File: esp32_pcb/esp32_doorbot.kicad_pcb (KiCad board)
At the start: 2 copper layers, 29.2 x 51.8 mm, 18 parts, among them J1 Conn_01x07_Male, J2 Conn_01x02_Female, J3 Barrel_Jack, J4 WROOM32_1, J5 WROOM32_2, Q1 2N7002E, U1 L7805, U2 74LVC2T45DC

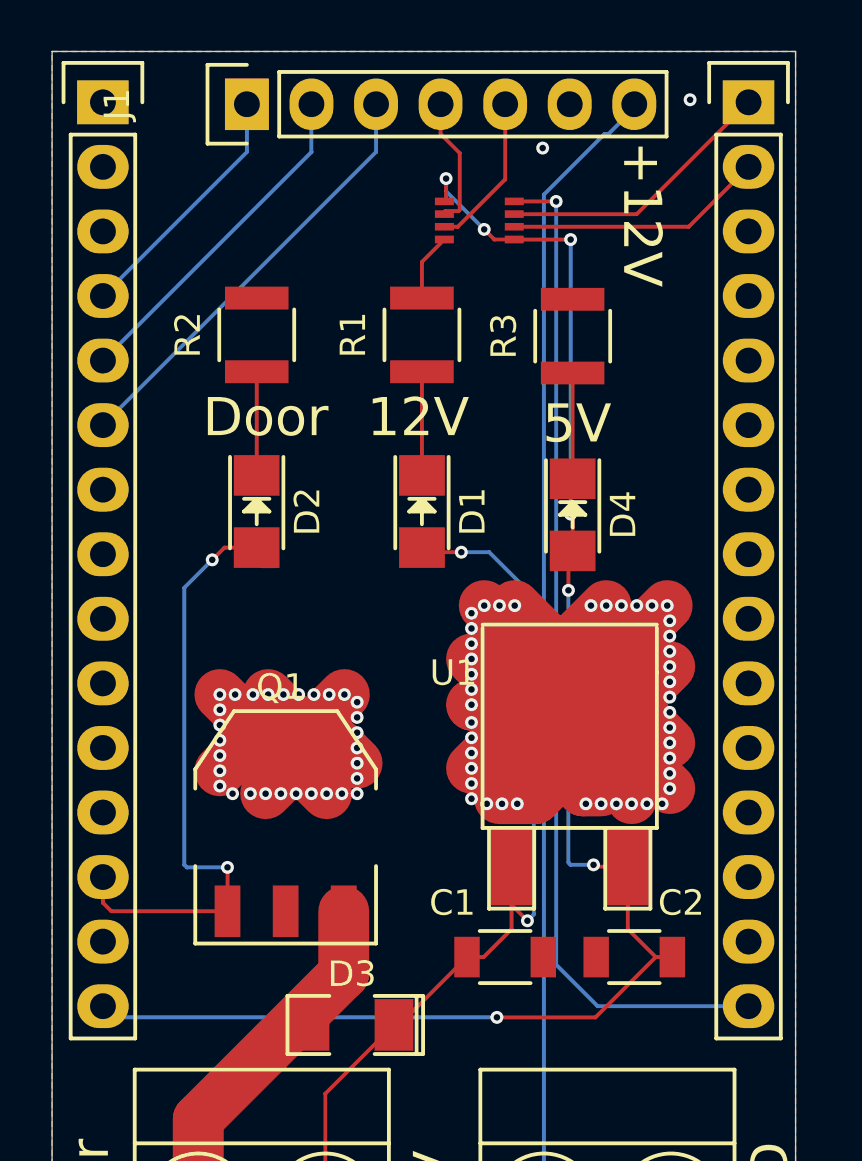
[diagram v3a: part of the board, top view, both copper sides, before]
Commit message: Switch to voltage divider instead of logic level converter
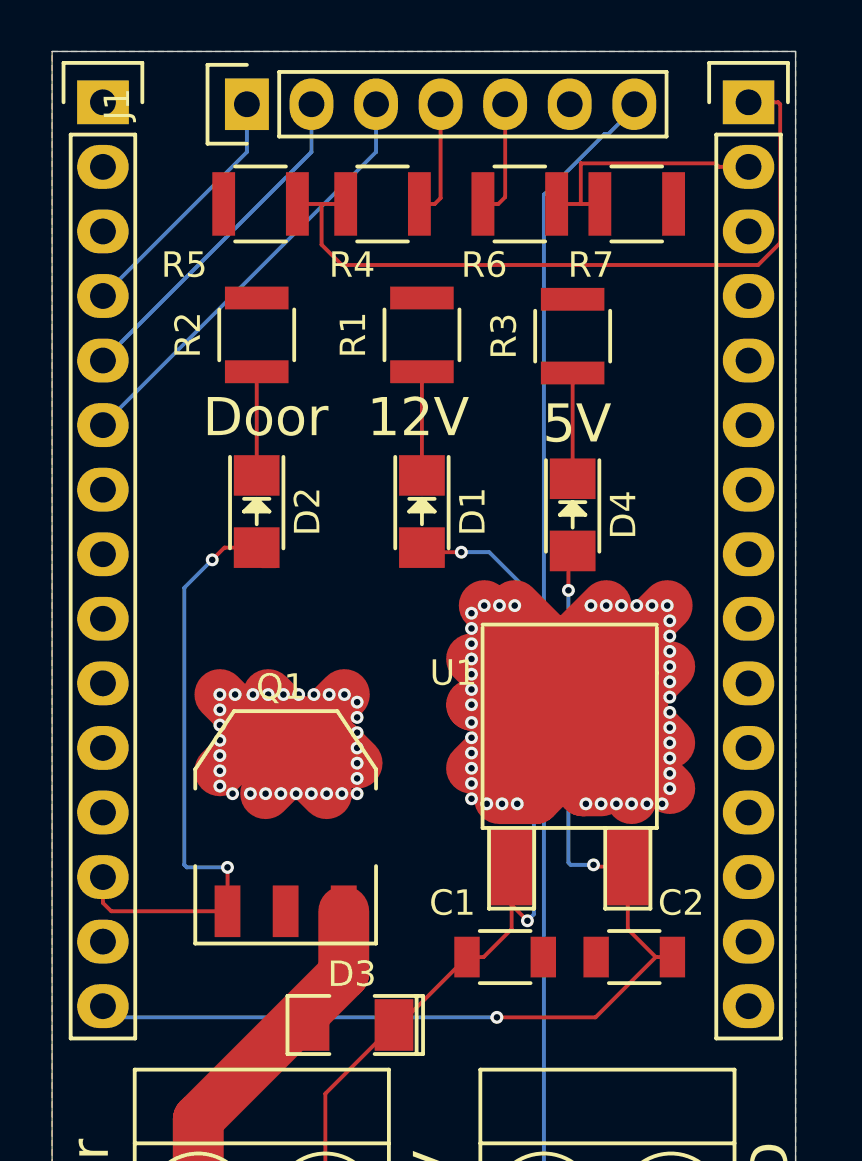
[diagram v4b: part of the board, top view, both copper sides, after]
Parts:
- removed REF**: Bodgery, custom:Bodgery
- removed U2: 74LVC2T45DC, tinkerforge-kicad:VSSOP8
- added R4: 1k, Resistors_SMD:R_1210, F.Cu at (111.0, 104.0)
- added R5: 2k, Resistors_SMD:R_1210, F.Cu at (106.2, 104.0)
- added R6: 1k, Resistors_SMD:R_1210, F.Cu at (116.4, 104.0)
- added R7: 2k, Resistors_SMD:R_1210, F.Cu at (121.0, 104.0)
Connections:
- J4 pad 1: Net-(J4-Pad1) -> (no net)
- J4 pad 10: Net-(J4-Pad10) -> (no net)
- J4 pad 11: Net-(J4-Pad11) -> (no net)
- J4 pad 12: Net-(J4-Pad12) -> (no net)
- J4 pad 2: Net-(J4-Pad2) -> (no net)
- J4 pad 3: Net-(J4-Pad3) -> (no net)
- J4 pad 7: Net-(J4-Pad7) -> (no net)
- J4 pad 8: Net-(J4-Pad8) -> (no net)
- J4 pad 9: Net-(J4-Pad9) -> (no net)
- J5 pad 10: Net-(J5-Pad10) -> (no net)
- J5 pad 11: Net-(J5-Pad11) -> (no net)
- J5 pad 12: Net-(J5-Pad12) -> (no net)
- J5 pad 13: Net-(J5-Pad13) -> (no net)
- J5 pad 15: 3.3V -> (no net)
- J5 pad 3: Net-(J5-Pad3) -> (no net)
- J5 pad 4: Net-(J5-Pad4) -> (no net)
- J5 pad 5: Net-(J5-Pad5) -> (no net)
- J5 pad 6: Net-(J5-Pad6) -> (no net)
- J5 pad 7: Net-(J5-Pad7) -> (no net)
- J5 pad 8: Net-(J5-Pad8) -> (no net)
- J5 pad 9: Net-(J5-Pad9) -> (no net)
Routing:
- net 3.3V: track 39.9 -> 0.00 mm, vias 1 -> 0
- net 5V: track 61.7 -> 42.3 mm, vias 7 -> 3
- net WIEGAND_OUT2: track 11.0 -> 29.0 mm
- net GND: track 85.1 -> 82.4 mm, vias 75 -> 73
- net WIEGAND_IN1: track 6.12 -> 4.64 mm
- net WIEGAND_IN2: track 5.19 -> 4.62 mm
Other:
- board text added: "ESP32 Doorbot v4 By Timm Murray Copyright © 2021 BY-CC"
- board text removed: "ESP32 Doorbot v3 By Timm Murray Copyright © 2021 BY-CC"

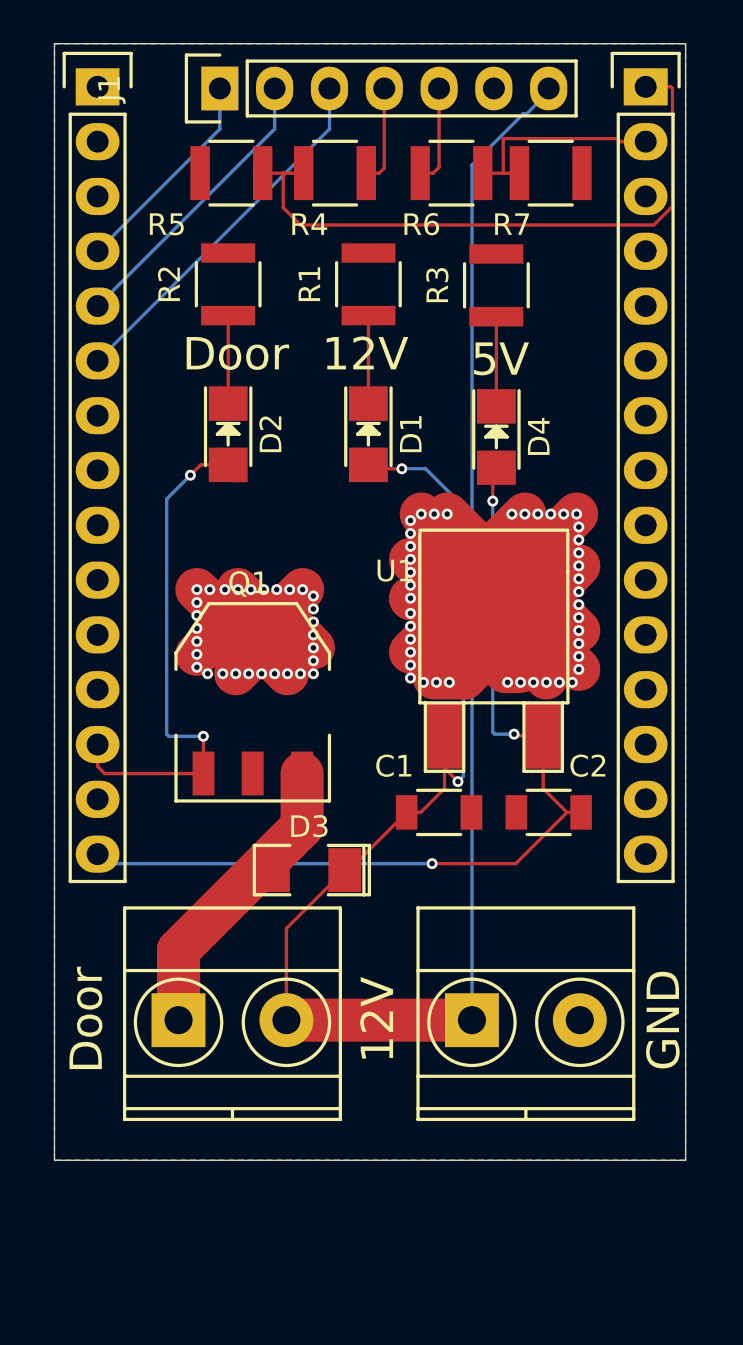
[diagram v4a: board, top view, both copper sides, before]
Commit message: Correct mosfet pinout (for real this time)
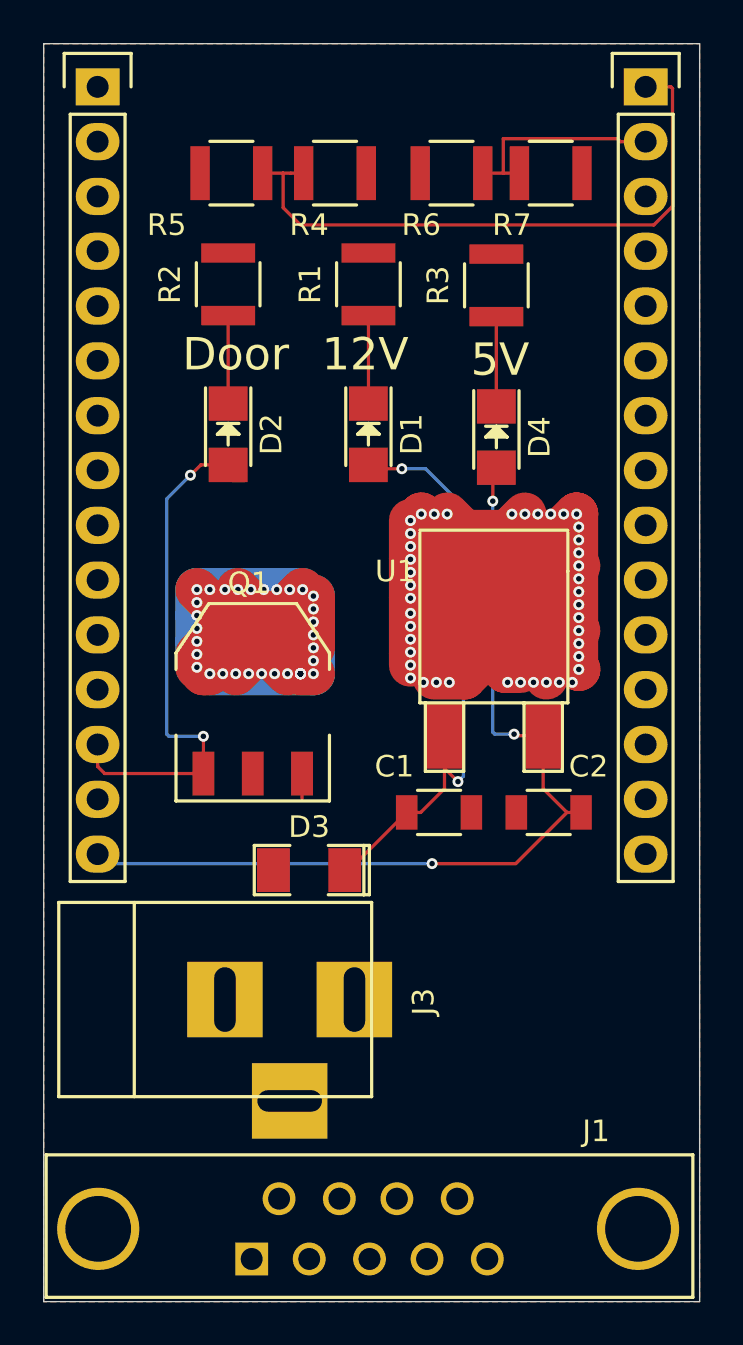
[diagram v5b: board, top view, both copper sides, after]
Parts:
- removed J2: Conn_01x02_Female, Terminal_Blocks:TerminalBlock_Pheonix_MKDS1.5-2pol
- J1: value Conn_01x07_Male -> DB9_Male; footprint Pin_Headers:Pin_Header_Straight_1x07 -> Connect:DB9FD
- J3: footprint Terminal_Blocks:TerminalBlock_Pheonix_MKDS1.5-2pol -> Connect:BARREL_JACK
- Q1: value 2N7002E -> ZVN4206GVTA
- moved J1 53.2 mm to (112.6, 152.8), turned to 180 degrees
- moved J3 11.7 mm to (105.7, 142.3)
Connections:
- J1 pad 1: 24_32_SWITCH -> 12V
- J1 pad 2: READER_LED -> 5V
- J1 pad 3: READER_BUZZ -> WIEGAND_IN1
- J1 pad 5: WIEGAND_IN1 -> GND
- J1 pad 7: 12V -> LATCH_OUT
- J4 pad 1: (no net) -> Net-(J4-Pad1)
- J4 pad 10: (no net) -> Net-(J4-Pad10)
- J4 pad 11: (no net) -> Net-(J4-Pad11)
- J4 pad 12: (no net) -> Net-(J4-Pad12)
- J4 pad 2: (no net) -> Net-(J4-Pad2)
- J4 pad 3: (no net) -> Net-(J4-Pad3)
- J4 pad 4: 24_32_SWITCH -> Net-(J4-Pad4)
- J4 pad 5: READER_LED -> Net-(J4-Pad5)
- J4 pad 7: (no net) -> Net-(J4-Pad7)
- J4 pad 8: (no net) -> Net-(J4-Pad8)
- J4 pad 9: (no net) -> Net-(J4-Pad9)
- J5 pad 10: (no net) -> Net-(J5-Pad10)
- J5 pad 11: (no net) -> Net-(J5-Pad11)
- J5 pad 12: (no net) -> Net-(J5-Pad12)
- J5 pad 13: (no net) -> Net-(J5-Pad13)
- J5 pad 15: (no net) -> Net-(J5-Pad15)
- J5 pad 3: (no net) -> Net-(J5-Pad3)
- J5 pad 4: (no net) -> Net-(J5-Pad4)
- J5 pad 5: (no net) -> Net-(J5-Pad5)
- J5 pad 6: (no net) -> Net-(J5-Pad6)
- J5 pad 7: (no net) -> Net-(J5-Pad7)
- J5 pad 8: (no net) -> Net-(J5-Pad8)
- J5 pad 9: (no net) -> Net-(J5-Pad9)
- Q1 pad 2: GND -> LATCH_OUT
- Q1 pad 3: LATCH_OUT -> GND
- Q1 pad 4: GND -> (no net)
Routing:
- net 12V: track 90.5 -> 29.1 mm
- net (no net): track 0.00 -> 51.3 mm, vias 0 -> 34
- net READER_BUZZ: track 17.1 -> 0.00 mm
- net LATCH_OUT: track 15.2 -> 0.00 mm
- net READER_LED: track 13.5 -> 0.00 mm
- net 24_32_SWITCH: track 10.4 -> 0.00 mm
- net WIEGAND_IN1: track 4.64 -> 0.00 mm
- net WIEGAND_IN2: track 4.62 -> 0.00 mm
- net GND: track 82.4 -> 85.6 mm, vias 73 -> 43
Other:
- board size 29.2 x 51.8 mm -> 30.4 x 58.3 mm
- board text removed: "+12V"
- board text removed: "GND"

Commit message: Revert "Correct mosfet pinout (for real this time)"
This reverts commit 8fe08cf28d7a1d30f1efb70a8aeb7666ade41443.
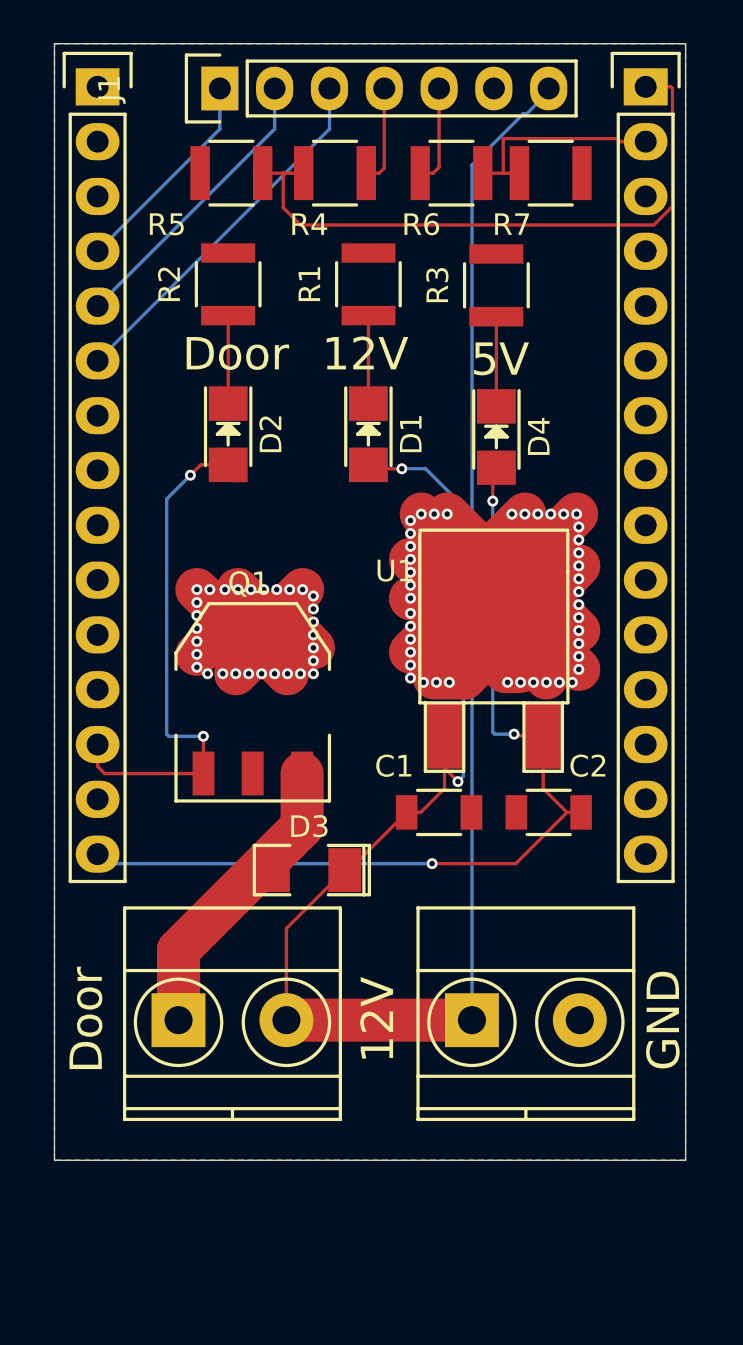
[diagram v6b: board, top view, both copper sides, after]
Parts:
- added J2: Conn_01x02_Female, Terminal_Blocks:TerminalBlock_Pheonix_MKDS1.5-2pol, F.Cu at (103.8, 143.3)
- J1: value DB9_Male -> Conn_01x07_Male; footprint Connect:DB9FD -> Pin_Headers:Pin_Header_Straight_1x07
- J3: footprint Connect:BARREL_JACK -> Terminal_Blocks:TerminalBlock_Pheonix_MKDS1.5-2pol
- Q1: value ZVN4206GVTA -> 2N7002E
- moved J1 53.2 mm to (105.7, 100.1), turned to 90 degrees
- moved J3 11.7 mm to (117.3, 143.3)
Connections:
- J1 pad 1: 12V -> 24_32_SWITCH
- J1 pad 2: 5V -> READER_LED
- J1 pad 3: WIEGAND_IN1 -> READER_BUZZ
- J1 pad 5: GND -> WIEGAND_IN1
- J1 pad 7: LATCH_OUT -> 12V
- J4 pad 1: Net-(J4-Pad1) -> (no net)
- J4 pad 10: Net-(J4-Pad10) -> (no net)
- J4 pad 11: Net-(J4-Pad11) -> (no net)
- J4 pad 12: Net-(J4-Pad12) -> (no net)
- J4 pad 2: Net-(J4-Pad2) -> (no net)
- J4 pad 3: Net-(J4-Pad3) -> (no net)
- J4 pad 4: Net-(J4-Pad4) -> 24_32_SWITCH
- J4 pad 5: Net-(J4-Pad5) -> READER_LED
- J4 pad 7: Net-(J4-Pad7) -> (no net)
- J4 pad 8: Net-(J4-Pad8) -> (no net)
- J4 pad 9: Net-(J4-Pad9) -> (no net)
- J5 pad 10: Net-(J5-Pad10) -> (no net)
- J5 pad 11: Net-(J5-Pad11) -> (no net)
- J5 pad 12: Net-(J5-Pad12) -> (no net)
- J5 pad 13: Net-(J5-Pad13) -> (no net)
- J5 pad 15: Net-(J5-Pad15) -> (no net)
- J5 pad 3: Net-(J5-Pad3) -> (no net)
- J5 pad 4: Net-(J5-Pad4) -> (no net)
- J5 pad 5: Net-(J5-Pad5) -> (no net)
- J5 pad 6: Net-(J5-Pad6) -> (no net)
- J5 pad 7: Net-(J5-Pad7) -> (no net)
- J5 pad 8: Net-(J5-Pad8) -> (no net)
- J5 pad 9: Net-(J5-Pad9) -> (no net)
- Q1 pad 2: LATCH_OUT -> GND
- Q1 pad 3: GND -> LATCH_OUT
- Q1 pad 4: (no net) -> GND
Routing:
- net 12V: track 29.1 -> 90.5 mm
- net (no net): track 51.3 -> 0.00 mm, vias 34 -> 0
- net READER_BUZZ: track 0.00 -> 17.1 mm
- net LATCH_OUT: track 0.00 -> 15.2 mm
- net READER_LED: track 0.00 -> 13.5 mm
- net 24_32_SWITCH: track 0.00 -> 10.4 mm
- net WIEGAND_IN1: track 0.00 -> 4.64 mm
- net WIEGAND_IN2: track 0.00 -> 4.62 mm
- net GND: track 85.6 -> 82.4 mm, vias 43 -> 73
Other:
- board size 30.4 x 58.3 mm -> 29.2 x 51.8 mm
- board text added: "+12V"
- board text added: "GND"

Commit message: Even more pinout corrections
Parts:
- Q1: value 2N7002E -> ZXMP4A16G
- moved C2 0.18 mm to (120.7, 133.6)
- moved Q1 0.14 mm to (107.3, 128.6)
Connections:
- J4 pad 1: (no net) -> Net-(J4-Pad1)
- J4 pad 10: (no net) -> Net-(J4-Pad10)
- J4 pad 11: (no net) -> Net-(J4-Pad11)
- J4 pad 12: (no net) -> Net-(J4-Pad12)
- J4 pad 2: (no net) -> Net-(J4-Pad2)
- J4 pad 3: (no net) -> Net-(J4-Pad3)
- J4 pad 7: (no net) -> Net-(J4-Pad7)
- J4 pad 8: (no net) -> Net-(J4-Pad8)
- J4 pad 9: (no net) -> Net-(J4-Pad9)
- J5 pad 10: (no net) -> Net-(J5-Pad10)
- J5 pad 11: (no net) -> Net-(J5-Pad11)
- J5 pad 12: (no net) -> Net-(J5-Pad12)
- J5 pad 13: (no net) -> Net-(J5-Pad13)
- J5 pad 15: (no net) -> Net-(J5-Pad15)
- J5 pad 3: (no net) -> Net-(J5-Pad3)
- J5 pad 4: (no net) -> Net-(J5-Pad4)
- J5 pad 5: (no net) -> Net-(J5-Pad5)
- J5 pad 6: (no net) -> Net-(J5-Pad6)
- J5 pad 7: (no net) -> Net-(J5-Pad7)
- J5 pad 8: (no net) -> Net-(J5-Pad8)
- J5 pad 9: (no net) -> Net-(J5-Pad9)
- Q1 pad 2: GND -> LATCH_OUT
- Q1 pad 3: LATCH_OUT -> GND
- Q1 pad 4: GND -> LATCH_OUT
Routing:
- net GND: track 82.4 -> 62.6 mm, vias 73 -> 43
- net LATCH_OUT: track 15.2 -> 20.1 mm

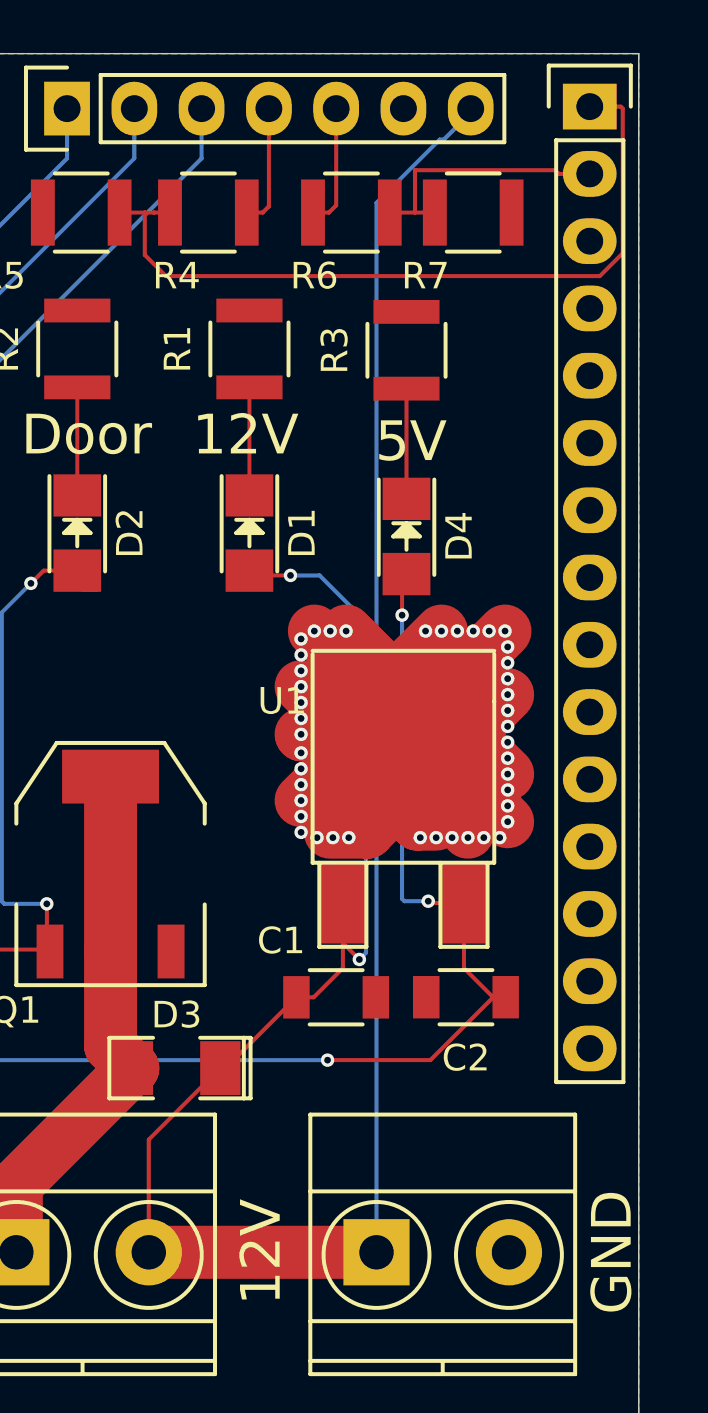
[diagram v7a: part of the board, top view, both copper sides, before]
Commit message: Use a through-hole buck converter
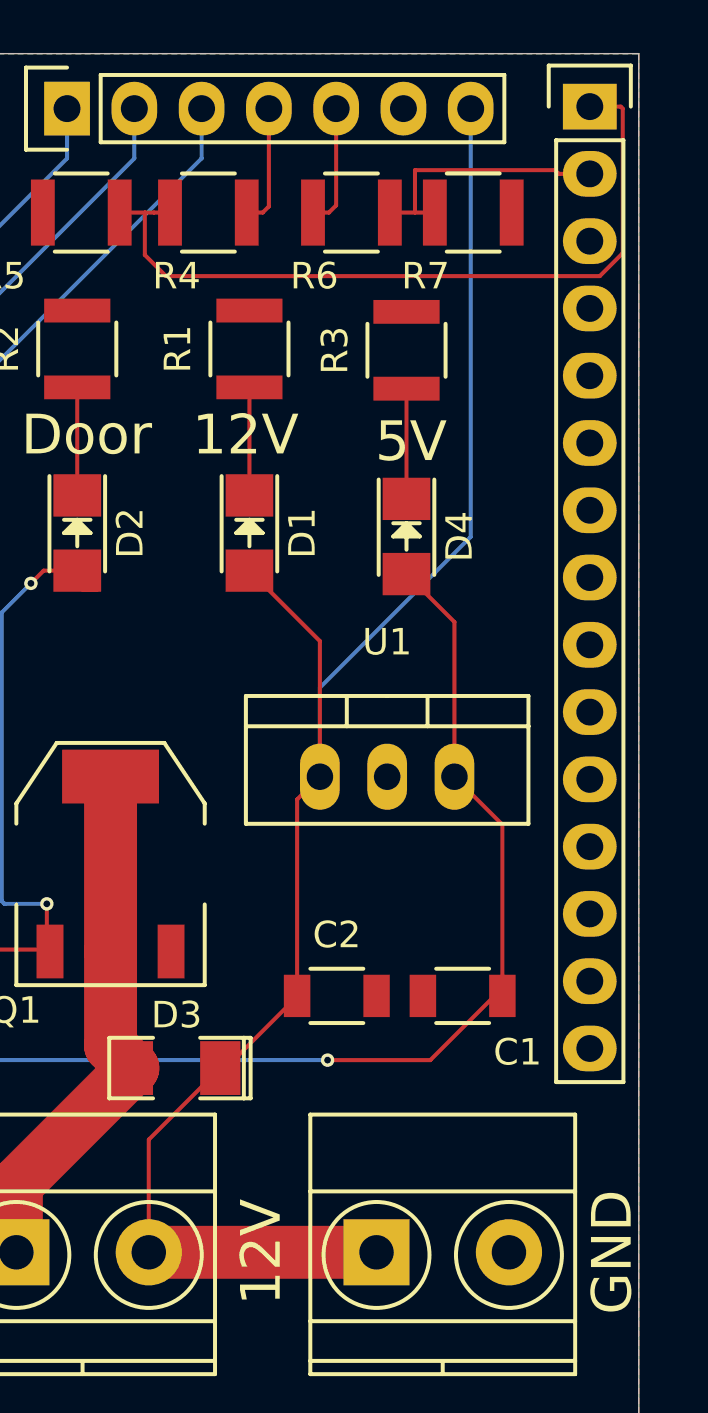
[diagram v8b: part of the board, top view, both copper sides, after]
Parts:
- C2: value 0.1uF -> 10uF
- U1: footprint TO_SOT_Packages_SMD:TO-252-2Lead -> TO_SOT_Packages_THT:TO-220_Neutral123_Vertical
- moved C2 4.88 mm to (115.8, 133.6), turned to 0 degrees
- moved U1 4.81 mm to (117.8, 125.3)
- moved C1 4.78 mm to (120.6, 133.6), turned to 180 degrees
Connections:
- C1 pad 1: 12V -> 5V
- C2 pad 1: 5V -> 12V
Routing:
- net GND: track 62.6 -> 0.00 mm, vias 43 -> 0
- net 12V: track 90.5 -> 65.7 mm, vias 2 -> 0
- net 5V: track 42.3 -> 41.0 mm, vias 3 -> 1
